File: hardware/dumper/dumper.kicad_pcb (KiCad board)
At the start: 2 copper layers, 90.2 x 55.9 mm, 27 parts, among them J1 /Reset, J10 arduino 10, J11 ss, J2 Clock In, J3 data, J4 clock, J5 2816 /WR disconnect, J6 arduino 13, J7 arduino 11, J8 arduino 5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

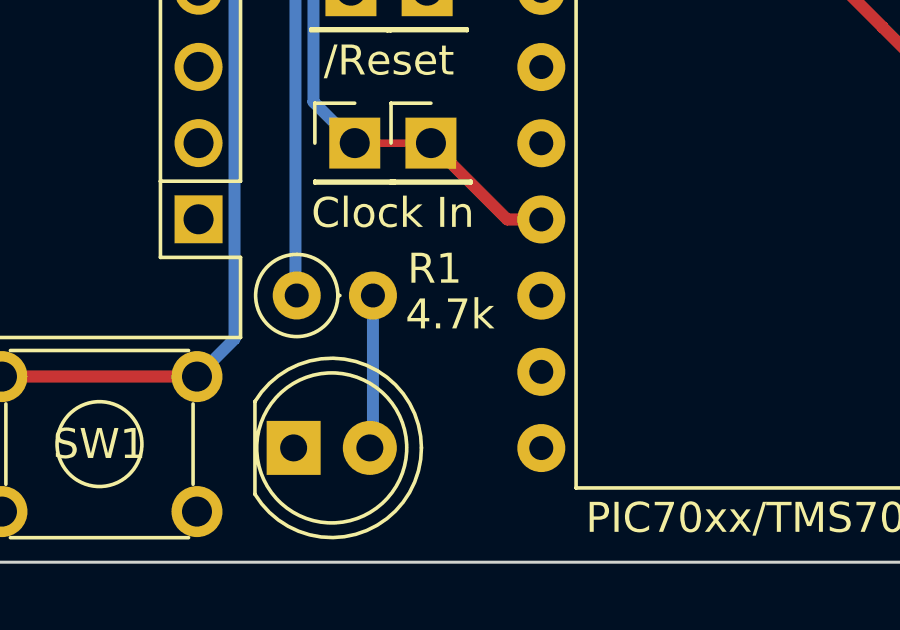
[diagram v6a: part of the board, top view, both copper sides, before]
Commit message: fixed resistor value for LED
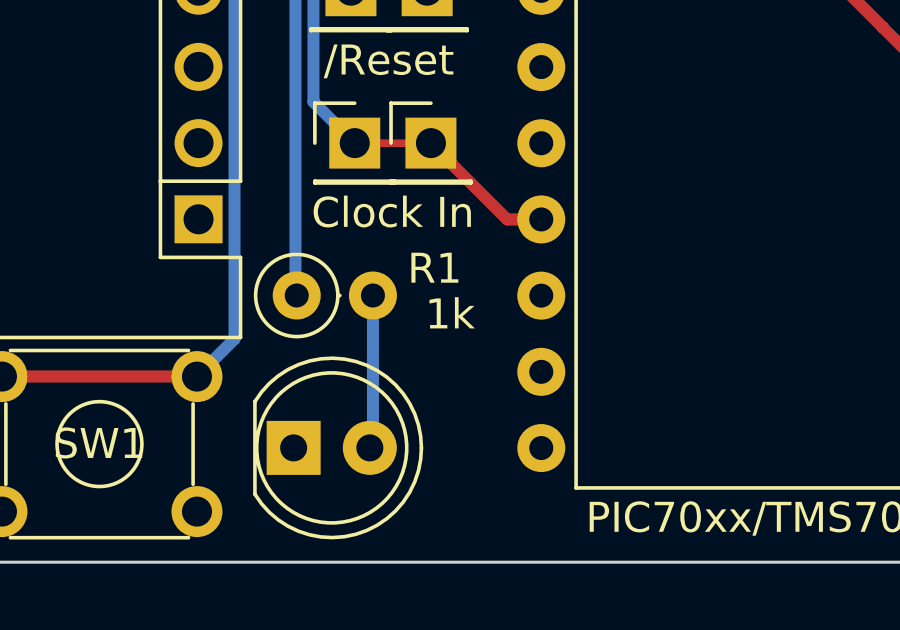
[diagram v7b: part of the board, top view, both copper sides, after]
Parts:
- R1: value 4.7k -> 1k
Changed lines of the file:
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@@
       (effects (font (size 1 1) (thickness 0.15)))
     )
-    (fp_text value "4.7k" (at 5.109 0.635) (layer "F.SilkS")
+    (fp_text value "1k" (at 5.109 0.635) (layer "F.SilkS")
       (effects (font (size 1 1) (thickness 0.15)))
     )

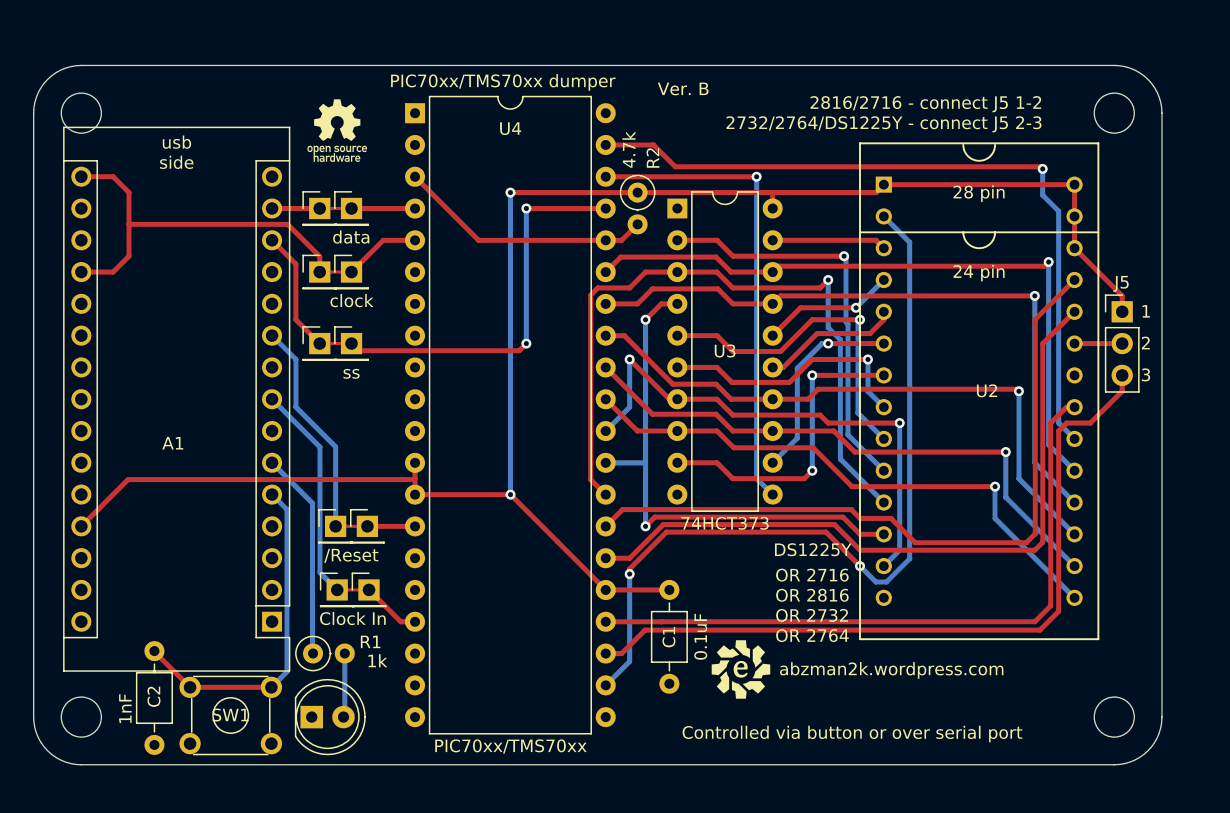
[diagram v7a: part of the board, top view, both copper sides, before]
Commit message: laid out rev b dumper
juggled all the address lines and additional arduino wiring to facilitate parallel reads and CT dumping
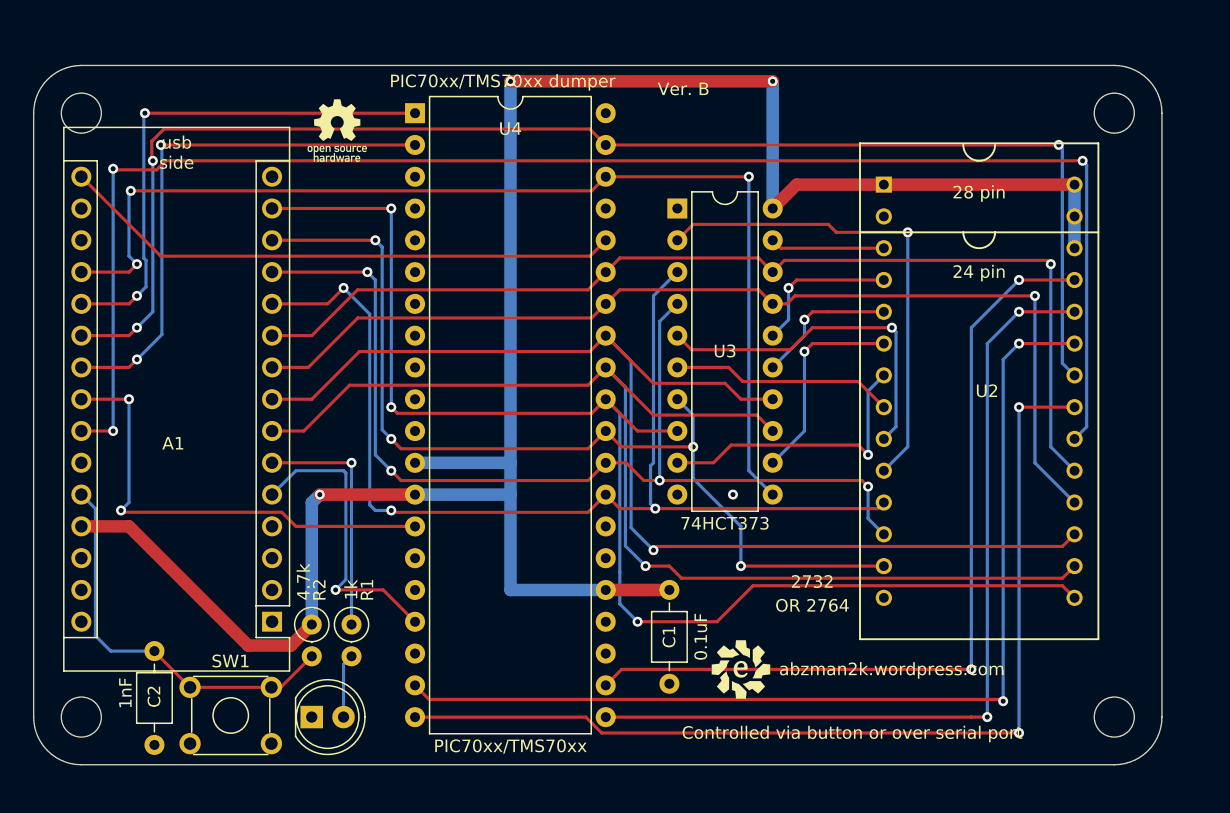
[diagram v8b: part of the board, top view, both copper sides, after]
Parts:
- removed J1: /Reset, Connector_PinHeader_2.54mm:PinHeader_1x01_P2.54mm_Vertical
- removed J10: arduino 10, Connector_PinHeader_2.54mm:PinHeader_1x01_P2.54mm_Vertical
- removed J11: ss, Connector_PinHeader_2.54mm:PinHeader_1x01_P2.54mm_Vertical
- removed J2: Clock In, Connector_PinHeader_2.54mm:PinHeader_1x01_P2.54mm_Vertical
- removed J3: data, Connector_PinHeader_2.54mm:PinHeader_1x01_P2.54mm_Vertical
- removed J4: clock, Connector_PinHeader_2.54mm:PinHeader_1x01_P2.54mm_Vertical
- removed J5: 2816 /WR disconnect, Connector_PinHeader_2.54mm:PinHeader_1x03_P2.54mm_Vertical
- removed J6: arduino 13, Connector_PinHeader_2.54mm:PinHeader_1x01_P2.54mm_Vertical
- removed J7: arduino 11, Connector_PinHeader_2.54mm:PinHeader_1x01_P2.54mm_Vertical
- removed J8: arduino 5, Connector_PinHeader_2.54mm:PinHeader_1x01_P2.54mm_Vertical
- removed J9: arduino 7, Connector_PinHeader_2.54mm:PinHeader_1x01_P2.54mm_Vertical
- U2: value DS1225Y -> 2732
- moved R2 43.2 mm to (96.5, 139.3)
- moved R1 3.85 mm to (99.7, 139.3), turned to -90 degrees
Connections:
- A1 pad 10: /RESET -> C7
- A1 pad 11: unconnected-(A1-Pad11) -> C0
- A1 pad 12: unconnected-(A1-Pad12) -> C1
- A1 pad 13: B3 -> C2
- A1 pad 14: B1 -> C3
- A1 pad 16: B2 -> MC
- A1 pad 19: B2 -> B4
- A1 pad 20: unconnected-(A1-Pad20) -> B5
- A1 pad 21: unconnected-(A1-Pad21) -> B6
- A1 pad 22: unconnected-(A1-Pad22) -> B7
- A1 pad 23: unconnected-(A1-Pad23) -> /RESET
- A1 pad 24: unconnected-(A1-Pad24) -> /READ
- A1 pad 26: unconnected-(A1-Pad26) -> Net-(A1-Pad26)
- A1 pad 5: Net-(A1-Pad5) -> XTAL2
- A1 pad 7: unconnected-(A1-Pad7) -> C4
- A1 pad 8: XTAL2 -> C5
- A1 pad 9: unconnected-(A1-Pad9) -> C6
- C2 pad 2: Net-(A1-Pad5) -> Net-(A1-Pad26)
- R2 pad 2: B0 -> Net-(A1-Pad26)
- SW1 pad 3: Net-(A1-Pad5) -> Net-(A1-Pad26)
- SW1 pad 4: Net-(A1-Pad5) -> Net-(A1-Pad26)
- U2 pad 2: D4 -> GND
- U2 pad 20: B6 -> /READ
- U2 pad 21: D2 -> D6
- U2 pad 22: GND -> B6
- U2 pad 23: Net-(J5-Pad2) -> D7
- U2 pad 24: D1 -> D5
- U2 pad 25: D0 -> D4
- U4 pad 36: B0 -> MC
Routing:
- net /READ: track 0.00 -> 124.1 mm, vias 0 -> 3
- net D7: track 0.00 -> 81.1 mm, vias 0 -> 2
- net D6: track 0.00 -> 79.3 mm, vias 0 -> 2
- net D5: track 0.00 -> 68.4 mm, vias 0 -> 2
- net C3: track 45.5 -> 105.3 mm, vias 1 -> 3
- net D3: track 59.7 -> 0.00 mm
- net D0: track 57.9 -> 0.00 mm
- net D1: track 56.6 -> 0.00 mm
- net B6: track 58.3 -> 112.5 mm, vias 1 -> 3
- net D2: track 53.1 -> 0.00 mm
- net C4: track 46.2 -> 96.5 mm
- net B4: track 38.0 -> 86.9 mm, vias 1 -> 3
- net C5: track 48.8 -> 97.1 mm
- net MC: track 0.00 -> 45.1 mm
- net B3: track 44.0 -> 0.00 mm, vias 2 -> 0
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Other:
- board text added: "Code loaded into the EPROM runs and dumps the internal code of the PIC7000 to the Arduino."
- board text added: "OR 2764"
- board text added: "a1"
- board text added: "a2"
- board text added: "a3"
- board text added: "a4"
- board text added: "a5"
- board text added: "a7"
- board text added: "d4"
- board text added: "d6"
- board text added: "d8"
- board text added: "d9"
- board text removed: "1"
- board text removed: "2"
- board text removed: "2816/2716 - connect J5 1-2 2732/2764/DS1225Y - connect J5 2-3"
- board text removed: "3"
- board text removed: "Code loaded into the EPROM/NVRAM runs and dumps the internal code of the PIC7000 to the Arduino."
- board text removed: "OR 2716 OR 2816 OR 2732 OR 2764"
